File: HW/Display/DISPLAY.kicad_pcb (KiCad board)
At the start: 2 copper layers, 100 x 45 mm, 21 parts, among them J1 IO, SW1 SW_PUSH, SW2 SW_PUSH, SW3 SW_PUSH, SW4 SW_PUSH, U1 ULN2003A, U2 HDSP-B09G, U3 MCP23017

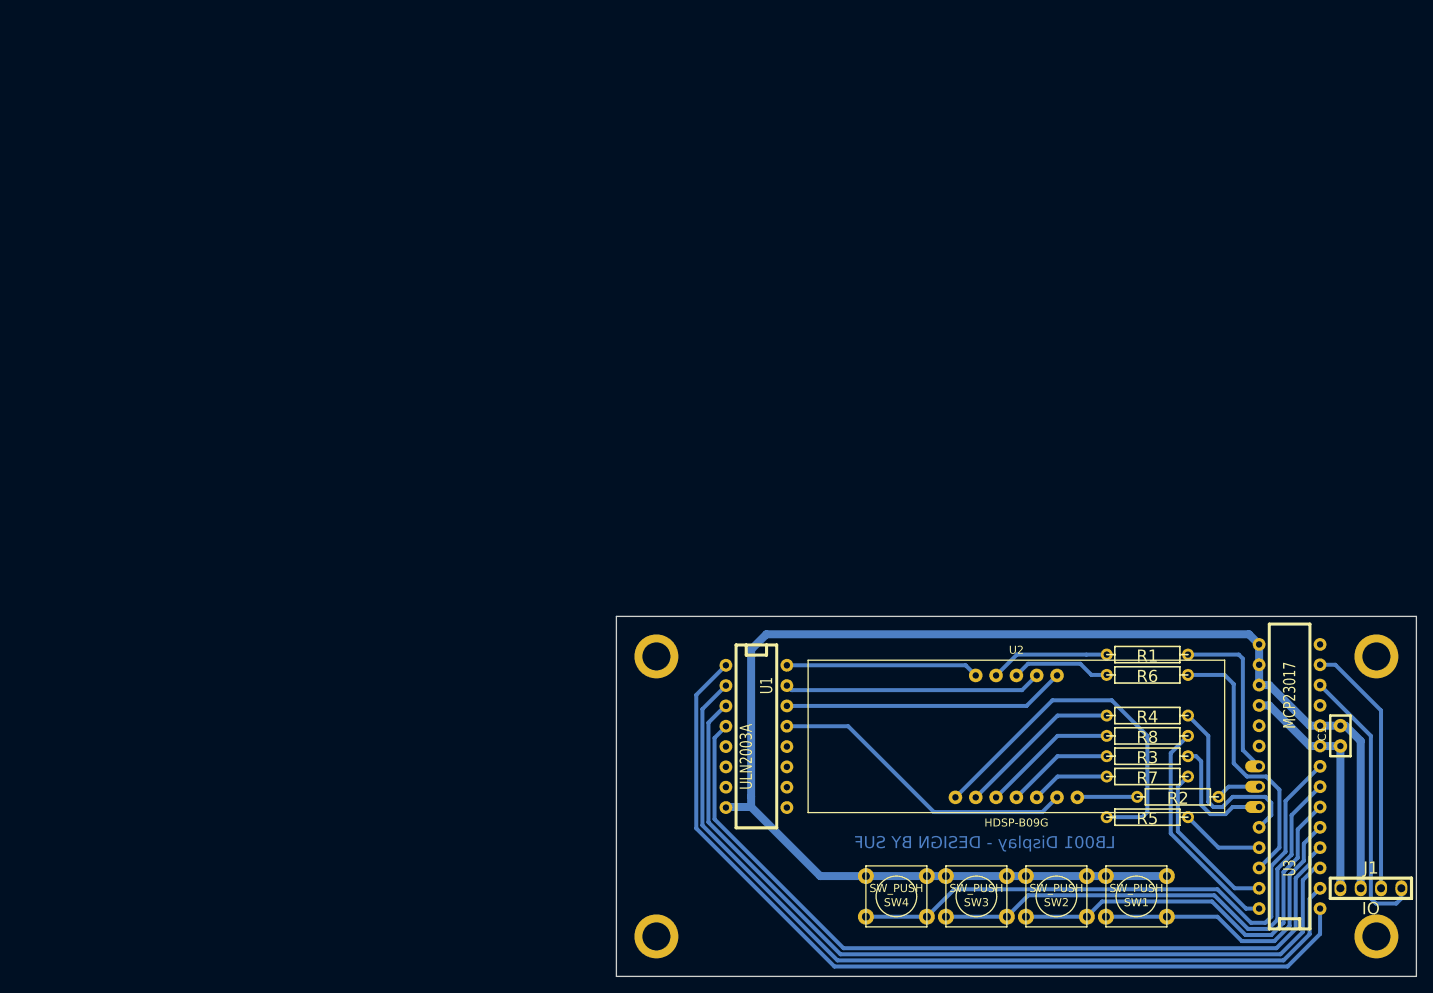
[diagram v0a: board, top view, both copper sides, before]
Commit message: Add Display design
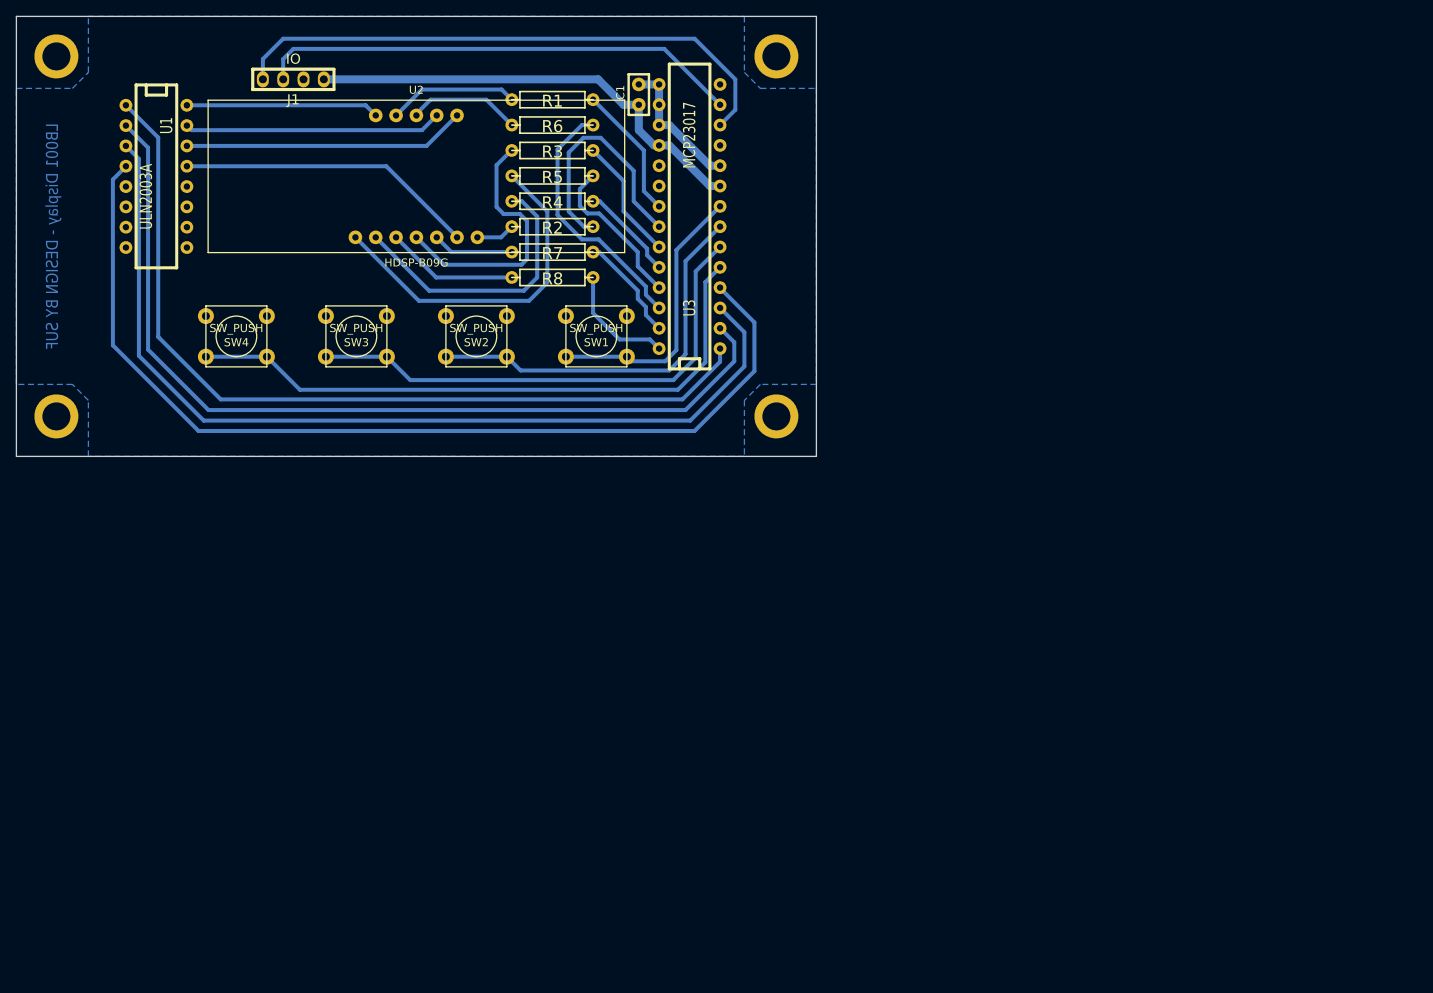
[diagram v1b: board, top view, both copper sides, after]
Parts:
- moved J1 168.4 mm to (59.6, 32.9), turned to 180 degrees
- moved C1 118.8 mm to (102.8, 34.8)
- moved R5 109.3 mm to (92.0, 44.9)
- moved SW4 108.2 mm to (52.5, 65.0)
- moved R3 106.1 mm to (92.0, 41.8)
- moved MNT_HOLE_3.5 106.1 mm to (30.0, 30.0)
- moved MNT_HOLE_3.5 106.1 mm to (120.0, 30.0)
- moved R2 105.8 mm to (92.0, 51.3)
- moved SW3 104.4 mm to (67.5, 65.0)
- moved U1 102.6 mm to (42.5, 45.0)
- moved U2 102.6 mm to (75.0, 45.0)
- moved U3 102.6 mm to (109.2, 50.0)
- moved R1 101.7 mm to (92.0, 35.4)
- moved R6 101.3 mm to (92.0, 38.6)
- moved SW2 100.8 mm to (82.5, 65.0)
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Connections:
- SW1 pad 1: N-0000017 -> Net-(SW1-Pad1)
- SW2 pad 1: N-0000016 -> Net-(SW2-Pad1)
- SW3 pad 1: N-0000015 -> Net-(SW3-Pad1)
- SW4 pad 1: N-0000018 -> Net-(SW4-Pad1)
- U1 pad 10: (no net) -> Net-(U1-Pad10)
- U1 pad 11: (no net) -> Net-(U1-Pad11)
- U1 pad 12: (no net) -> Net-(U1-Pad12)
- U1 pad 5: (no net) -> Net-(U1-Pad5)
- U1 pad 6: (no net) -> Net-(U1-Pad6)
- U1 pad 7: (no net) -> Net-(U1-Pad7)
- U1 pad 8: GND -> Net-(U1-Pad8)
- U1 pad 9: (no net) -> Net-(U1-Pad9)
- U3 pad 19: (no net) -> Net-(U3-Pad19)
- U3 pad 20: (no net) -> Net-(U3-Pad20)
- U3 pad 5: N-0000017 -> Net-(SW4-Pad1)
- U3 pad 6: N-0000016 -> Net-(SW3-Pad1)
- U3 pad 7: N-0000015 -> Net-(SW2-Pad1)
- U3 pad 8: N-0000018 -> Net-(SW1-Pad1)
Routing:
- net GND: track 182.3 -> 17.3 mm
- net Net-(SW4-Pad1): track 0.00 -> 78.2 mm
- net N-0000018: track 75.5 -> 0.00 mm
- net Net-(SW3-Pad1): track 0.00 -> 63.7 mm
- net N-0000015: track 63.6 -> 0.00 mm
- net N-0000016: track 51.7 -> 0.00 mm
- net Net-(SW2-Pad1): track 0.00 -> 49.2 mm
- net N-0000017: track 38.9 -> 0.00 mm
- net Net-(J1-Pad4): track 34.9 -> 71.3 mm
- net Net-(SW1-Pad1): track 0.00 -> 34.9 mm
- net Net-(J1-Pad3): track 32.2 -> 60.6 mm
- net VCC: track 30.0 -> 56.9 mm
- net Net-(R2-Pad2): track 5.61 -> 30.1 mm
- net Net-(R3-Pad1): track 13.4 -> 32.7 mm
- net Net-(U1-Pad4): track 104.0 -> 123.0 mm
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- added copper zone on B.Cu, net GND
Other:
- board size 100 x 45 mm -> 100 x 55 mm
